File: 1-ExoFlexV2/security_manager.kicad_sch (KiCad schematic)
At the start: 5 parts, among them U15 OR GATE 3IN, U8 OR Gate 8, U9 OR Gate 8

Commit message: PLacement 2
- Puissance
- signaux
-
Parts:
- added J82: Jumper, Connector_PinHeader_2.54mm:PinHeader_1x03_P2.54mm_Vertical, symbol Connector:Conn_01x03_Male
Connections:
- net ALIM_SEC: now also J82.2 (Pin_2); no longer TP24.TP, U15.4 (Y)
- net GND: now also J82.3 (Pin_3)
- new net: J82.1 (Pin_1), TP24.TP, U15.4 (Y)
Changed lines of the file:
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@@
 (kicad_sch (version 20211123) (generator eeschema)
   (paper "A4")
+  (junction (at 228.6 93.98) (diameter 0) (color 0 0 0 0)
+  )
   (junction (at 130.81 121.92) (diameter 0) (color 0 0 0 0)
-  )
-  (junction (at 228.6 93.98) (diameter 0) (color 0 0 0 0)
   )
   (junction (at 130.81 124.46) (diameter 0) (color 0 0 0 0)
@@
     (stroke (width 0) (type default) (color 0 0 0 0))
   )
+  (wire (pts (xy 243.84 93.98) (xy 243.84 97.79))
+    (stroke (width 0) (type default) (color 0 0 0 0))
+  )
   (wire (pts (xy 77.47 120.65) (xy 87.63 120.65))
     (stroke (width 0) (type default) (color 0 0 0 0))
@@
   )
   (wire (pts (xy 182.88 73.66) (xy 182.88 91.44))
+    (stroke (width 0) (type default) (color 0 0 0 0))
+  )
+  (wire (pts (xy 246.38 97.79) (xy 251.46 97.79))
     (stroke (width 0) (type default) (color 0 0 0 0))
   )
@@
     (stroke (width 0.5) (type dash) (color 54 168 53 1))
   )
+  (wire (pts (xy 241.3 93.98) (xy 228.6 93.98))
+    (stroke (width 0) (type default) (color 0 0 0 0))
+  )
   (wire (pts (xy 77.47 67.31) (xy 82.55 67.31))
     (stroke (width 0) (type default) (color 0 0 0 0))
@@
     (stroke (width 0) (type default) (color 0 0 0 0))
   )
+  (wire (pts (xy 241.3 97.79) (xy 241.3 93.98))
+    (stroke (width 0) (type default) (color 0 0 0 0))
+  )
   (wire (pts (xy 130.81 119.38) (xy 132.08 119.38))
     (stroke (width 0) (type default) (color 0 0 0 0))
@@
   )
   (wire (pts (xy 149.86 106.68) (xy 152.4 106.68))
-    (stroke (width 0) (type default) (color 0 0 0 0))
-  )
-  (wire (pts (xy 228.6 93.98) (xy 238.76 93.98))
     (stroke (width 0) (type default) (color 0 0 0 0))
   )
@@
     )
   )
-  (global_label "ALIM_SEC" (shape input) (at 238.76 93.98 0) (fields_autoplaced)
+  (global_label "ALIM_SEC" (shape input) (at 243.84 93.98 0) (fields_autoplaced)
     (effects (font (size 1.27 1.27) (thickness 0.254) bold) (justify left))
-    (property "Intersheet References" "${INTERSHEET_REFS}" (id 0) (at 250.323 93.853 0)
+    (property "Intersheet References" "${INTERSHEET_REFS}" (id 0) (at 255.403 93.853 0)
       (effects (font (size 1.27 1.27) (thickness 0.254) bold) (justify left) hide)
     )
@@
       (effects (font (size 1.27 1.27)) hide)
     )
+    (pin "1")
+  )
+  (symbol (lib_id "Connector:Conn_01x03_Male") (at 243.84 102.87 90) (unit 1)
+    (in_bom yes) (on_board yes)
+    (property "Reference" "J82" (id 0) (at 238.76 101.6 90))
+    (property "Value" "Jumper" (id 1) (at 243.84 104.14 90))
+    (property "Footprint" "Connector_PinHeader_2.54mm:PinHeader_1x03_P2.54mm_Vertical" (id 2) (at 243.84 102.87 0)
+      (effects (font (size 1.27 1.27)) hide)
+    )
+    (property "Datasheet" "~" (id 3) (at 243.84 102.87 0)
+      (effects (font (size 1.27 1.27)) hide)
+    )
+    (property "DESCRIPTION" "CONN HEADER VERT 3POS 2.54MM" (id 4) (at 243.84 102.87 0)
+      (effects (font (size 1.27 1.27)) hide)
+    )
+    (property "MANUFACTURER" "Würth Elektronik" (id 5) (at 243.84 102.87 0)
+      (effects (font (size 1.27 1.27)) hide)
+    )
+    (property "PACKAGE" "Square 0.100\" (2.54mm)" (id 6) (at 243.84 102.87 0)
+      (effects (font (size 1.27 1.27)) hide)
+    )
+    (property "PART NUMBER" "61300311121" (id 7) (at 243.84 102.87 0)
+      (effects (font (size 1.27 1.27)) hide)
+    )
+    (property "TYPE" "Through Hole" (id 8) (at 243.84 102.87 0)
+      (effects (font (size 1.27 1.27)) hide)
+    )
+    (pin "1")
+    (pin "2")
+    (pin "3")
+  )
+  (symbol (lib_id "power:GND") (at 251.46 97.79 0) (unit 1)
+    (in_bom yes) (on_board yes)
+    (property "Reference" "#PWR0521" (id 0) (at 251.46 104.14 0)
+      (effects (font (size 1.27 1.27)) hide)
+    )
+    (property "Value" "GND" (id 1) (at 251.46 101.6 0))
+    (property "Footprint" "" (id 2) (at 251.46 97.79 0)
+      (effects (font (size 1.27 1.27)) hide)
+    )
+    (property "Datasheet" "" (id 3) (at 251.46 97.79 0)
+      (effects (font (size 1.27 1.27)) hide)
+    )

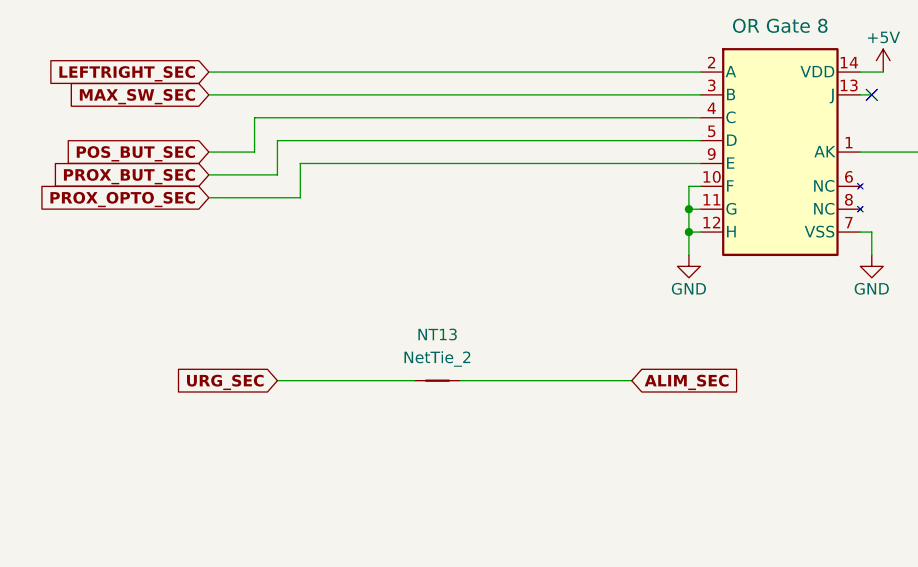
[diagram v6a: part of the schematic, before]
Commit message: Routage Fin
- Alimentation router
- Urg Sec dans le OR gate vers Alim Sec
- Changement d'un condo
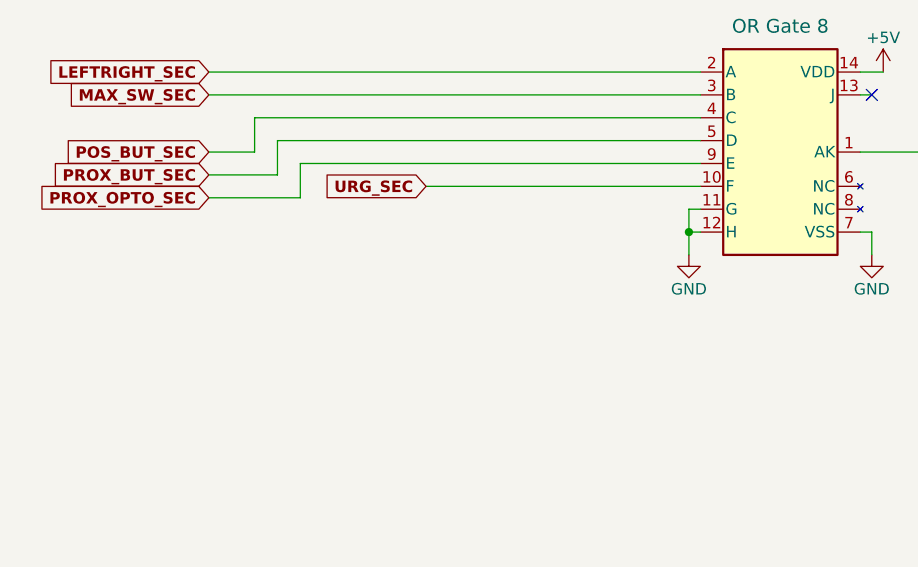
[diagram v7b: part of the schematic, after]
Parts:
- removed NT13: NetTie_2, NetTie:NetTie-2_THT_Pad0.3mm, symbol Device:NetTie_2
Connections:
- net GND: no longer U9.10 (F)
- net URG_SEC: now also U9.10 (F)
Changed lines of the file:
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@@
   (junction (at 228.6 93.98) (diameter 0) (color 0 0 0 0)
-  )
-  (junction (at 130.81 121.92) (diameter 0) (color 0 0 0 0)
   )
   (junction (at 130.81 124.46) (diameter 0) (color 0 0 0 0)
@@
     (stroke (width 0) (type default) (color 0 0 0 0))
   )
-  (wire (pts (xy 130.81 121.92) (xy 130.81 119.38))
-    (stroke (width 0) (type default) (color 0 0 0 0))
-  )
   (wire (pts (xy 80.01 69.85) (xy 80.01 72.39))
     (stroke (width 0) (type default) (color 0 0 0 0))
@@
     (stroke (width 0) (type default) (color 0 0 0 0))
   )
-  (wire (pts (xy 105.41 140.97) (xy 124.46 140.97))
-    (stroke (width 0) (type default) (color 0 0 0 0))
-  )
   (wire (pts (xy 151.13 109.22) (xy 149.86 109.22))
     (stroke (width 0) (type default) (color 0 0 0 0))
@@
   )
   (wire (pts (xy 241.3 97.79) (xy 241.3 93.98))
-    (stroke (width 0) (type default) (color 0 0 0 0))
-  )
-  (wire (pts (xy 130.81 119.38) (xy 132.08 119.38))
     (stroke (width 0) (type default) (color 0 0 0 0))
   )
@@
     (stroke (width 0.5) (type dash) (color 54 168 53 1))
   )
-  (wire (pts (xy 85.09 140.97) (xy 100.33 140.97))
+  (wire (pts (xy 101.6 119.38) (xy 132.08 119.38))
     (stroke (width 0) (type default) (color 0 0 0 0))
   )
@@
     )
   )
-  (global_label "URG_SEC" (shape input) (at 85.09 140.97 180) (fields_autoplaced)
-    (effects (font (size 1.27 1.27) (thickness 0.254) bold) (justify right))
-    (property "Intersheet References" "${INTERSHEET_REFS}" (id 0) (at 73.8293 141.097 0)
+  (global_label "URG_SEC" (shape input) (at 101.6 119.38 180) (fields_autoplaced)
+    (effects (font (size 1.27 1.27) (thickness 0.254) bold) (justify right))
+    (property "Intersheet References" "${INTERSHEET_REFS}" (id 0) (at 90.3393 119.507 0)
       (effects (font (size 1.27 1.27) (thickness 0.254) bold) (justify right) hide)
     )
@@
     (effects (font (size 1.27 1.27) (thickness 0.254) bold) (justify left))
     (property "Intersheet References" "${INTERSHEET_REFS}" (id 0) (at 255.403 93.853 0)
-      (effects (font (size 1.27 1.27) (thickness 0.254) bold) (justify left) hide)
-    )
-  )
-  (global_label "ALIM_SEC" (shape input) (at 124.46 140.97 0) (fields_autoplaced)
-    (effects (font (size 1.27 1.27) (thickness 0.254) bold) (justify left))
-    (property "Intersheet References" "${INTERSHEET_REFS}" (id 0) (at 136.023 140.843 0)
       (effects (font (size 1.27 1.27) (thickness 0.254) bold) (justify left) hide)
     )
@@
     (pin "1")
   )
-  (symbol (lib_id "Device:NetTie_2") (at 102.87 140.97 0) (unit 1)
-    (in_bom no) (on_board yes) (fields_autoplaced)
-    (property "Reference" "NT13" (id 0) (at 102.87 135.89 0))
-    (property "Value" "NetTie_2" (id 1) (at 102.87 138.43 0))
-    (property "Footprint" "NetTie:NetTie-2_THT_Pad0.3mm" (id 2) (at 102.87 140.97 0)
-      (effects (font (size 1.27 1.27)) hide)
-    )
-    (property "Datasheet" "~" (id 3) (at 102.87 140.97 0)
-      (effects (font (size 1.27 1.27)) hide)
-    )
-    (pin "1")
-    (pin "2")
-  )
   (symbol (lib_id "power:GND") (at 130.81 127 0) (unit 1)

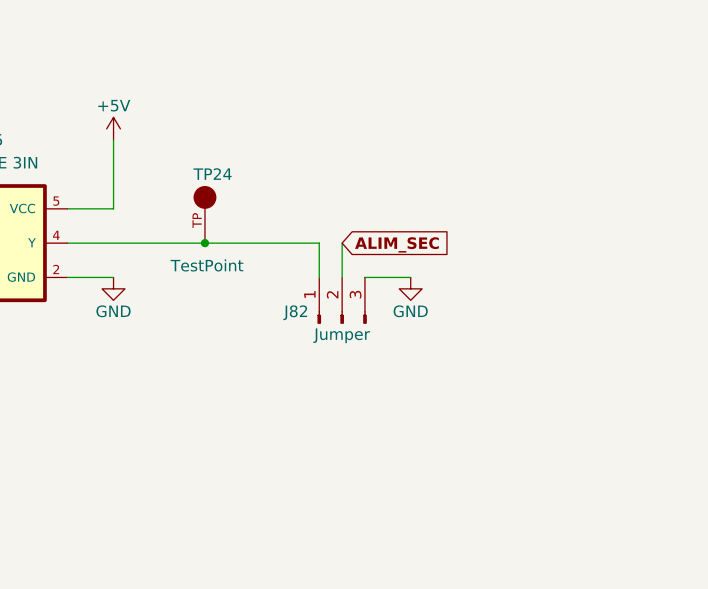
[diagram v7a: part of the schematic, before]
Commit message: Routage pour Review 1
- Replacement des test point pour faciliter le rework
- Correction des erreurs dans le BOM
-
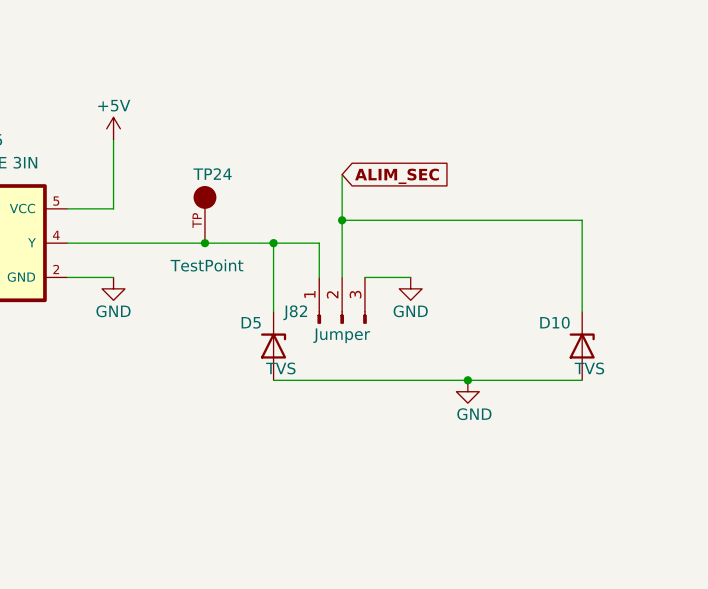
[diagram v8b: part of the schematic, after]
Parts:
- added D10, D5: TVS, FootPrint:DPY2_TEX, symbol Device:D_Zener
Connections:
- net ALIM_SEC: now also D10.1 (K)
- net GND: now also D10.2 (A), D5.2 (A)
- net at J82.1 (Pin_1), TP24.TP, U15.4 (Y): now also D5.1 (K)
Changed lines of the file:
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@@
 (kicad_sch (version 20211123) (generator eeschema)
   (paper "A4")
+  (junction (at 243.84 91.44) (diameter 0) (color 0 0 0 0)
+  )
   (junction (at 228.6 93.98) (diameter 0) (color 0 0 0 0)
+  )
+  (junction (at 236.22 93.98) (diameter 0) (color 0 0 0 0)
+  )
+  (junction (at 257.81 109.22) (diameter 0) (color 0 0 0 0)
   )
   (junction (at 130.81 124.46) (diameter 0) (color 0 0 0 0)
@@
   (no_connect (at 151.13 109.22))
   (no_connect (at 149.86 67.31))
+  (wire (pts (xy 270.51 101.6) (xy 270.51 91.44))
+    (stroke (width 0) (type default) (color 0 0 0 0))
+  )
   (wire (pts (xy 130.81 124.46) (xy 132.08 124.46))
     (stroke (width 0) (type default) (color 0 0 0 0))
   )
-  (wire (pts (xy 243.84 93.98) (xy 243.84 97.79))
+  (wire (pts (xy 243.84 86.36) (xy 243.84 91.44))
     (stroke (width 0) (type default) (color 0 0 0 0))
   )
@@
     (stroke (width 0) (type default) (color 0 0 0 0))
   )
+  (wire (pts (xy 236.22 109.22) (xy 257.81 109.22))
+    (stroke (width 0) (type default) (color 0 0 0 0))
+  )
+  (wire (pts (xy 243.84 91.44) (xy 270.51 91.44))
+    (stroke (width 0) (type default) (color 0 0 0 0))
+  )
   (wire (pts (xy 87.63 120.65) (xy 87.63 116.84))
     (stroke (width 0) (type default) (color 0 0 0 0))
@@
   )
   (wire (pts (xy 182.88 73.66) (xy 182.88 91.44))
+    (stroke (width 0) (type default) (color 0 0 0 0))
+  )
+  (wire (pts (xy 243.84 91.44) (xy 243.84 97.79))
     (stroke (width 0) (type default) (color 0 0 0 0))
   )
@@
     (stroke (width 0.5) (type dash) (color 54 168 53 1))
   )
-  (wire (pts (xy 241.3 93.98) (xy 228.6 93.98))
-    (stroke (width 0) (type default) (color 0 0 0 0))
-  )
   (wire (pts (xy 77.47 67.31) (xy 82.55 67.31))
     (stroke (width 0) (type default) (color 0 0 0 0))
@@
     (stroke (width 0) (type default) (color 0 0 0 0))
   )
+  (wire (pts (xy 257.81 109.22) (xy 270.51 109.22))
+    (stroke (width 0) (type default) (color 0 0 0 0))
+  )
   (wire (pts (xy 213.36 93.98) (xy 228.6 93.98))
     (stroke (width 0) (type default) (color 0 0 0 0))
@@
   )
   (wire (pts (xy 77.47 80.01) (xy 82.55 80.01))
+    (stroke (width 0) (type default) (color 0 0 0 0))
+  )
+  (wire (pts (xy 236.22 93.98) (xy 228.6 93.98))
     (stroke (width 0) (type default) (color 0 0 0 0))
   )
@@
     (stroke (width 0) (type default) (color 0 0 0 0))
   )
-  (wire (pts (xy 241.3 97.79) (xy 241.3 93.98))
+  (wire (pts (xy 241.3 93.98) (xy 241.3 97.79))
     (stroke (width 0) (type default) (color 0 0 0 0))
   )
@@
     (stroke (width 0.5) (type dash) (color 54 168 53 1))
   )
+  (wire (pts (xy 236.22 101.6) (xy 236.22 93.98))
+    (stroke (width 0) (type default) (color 0 0 0 0))
+  )
   (wire (pts (xy 87.63 116.84) (xy 132.08 116.84))
     (stroke (width 0) (type default) (color 0 0 0 0))
@@
   )
   (wire (pts (xy 77.47 88.9) (xy 87.63 88.9))
+    (stroke (width 0) (type default) (color 0 0 0 0))
+  )
+  (wire (pts (xy 236.22 93.98) (xy 241.3 93.98))
     (stroke (width 0) (type default) (color 0 0 0 0))
   )
@@
     )
   )
-  (global_label "ALIM_SEC" (shape input) (at 243.84 93.98 0) (fields_autoplaced)
+  (global_label "ALIM_SEC" (shape input) (at 243.84 86.36 0) (fields_autoplaced)
     (effects (font (size 1.27 1.27) (thickness 0.254) bold) (justify left))
-    (property "Intersheet References" "${INTERSHEET_REFS}" (id 0) (at 255.403 93.853 0)
+    (property "Intersheet References" "${INTERSHEET_REFS}" (id 0) (at 255.403 86.233 0)
       (effects (font (size 1.27 1.27) (thickness 0.254) bold) (justify left) hide)
     )
@@
     (pin "9")
   )
+  (symbol (lib_id "power:GND") (at 257.81 109.22 0) (unit 1)
+    (in_bom yes) (on_board yes)
+    (property "Reference" "#PWR0339" (id 0) (at 257.81 115.57 0)
+      (effects (font (size 1.27 1.27)) hide)
+    )
+    (property "Value" "GND" (id 1) (at 256.54 113.03 0)
+      (effects (font (size 1.27 1.27)) (justify left))
+    )
+    (property "Footprint" "" (id 2) (at 257.81 109.22 0)
+      (effects (font (size 1.27 1.27)) hide)
+    )
+    (property "Datasheet" "" (id 3) (at 257.81 109.22 0)
+      (effects (font (size 1.27 1.27)) hide)
+    )
+    (pin "1")
+  )
   (symbol (lib_id "SymLib:SN74LVC1G332DBVR") (at 204.47 99.06 0) (unit 1)
     (in_bom yes) (on_board yes) (fields_autoplaced)
@@
     (pin "1")
   )
+  (symbol (lib_id "Device:D_Zener") (at 270.51 105.41 270) (unit 1)
+    (in_bom yes) (on_board yes)
+    (property "Reference" "D10" (id 0) (at 269.24 102.87 90)
+      (effects (font (size 1.27 1.27)) (justify right))
+    )
+    (property "Value" "TVS" (id 1) (at 273.05 107.95 90)
+      (effects (font (size 1.27 1.27)) (justify right))
+    )
+    (property "Footprint" "FootPrint:DPY2_TEX" (id 2) (at 270.51 105.41 0)
+      (effects (font (size 1.27 1.27)) hide)
+    )
+    (property "Datasheet" "~" (id 3) (at 270.51 105.41 0)
+      (effects (font (size 1.27 1.27)) hide)
+    )
+    (property "DESCRIPTION" "TVS DIODE 5.5VWM 14VC 2X1SON" (id 4) (at 270.51 105.41 0)
+      (effects (font (size 1.27 1.27)) hide)
+    )
+    (property "MANUFACTURER" "Texas Instruments" (id 5) (at 270.51 105.41 0)
+      (effects (font (size 1.27 1.27)) hide)
+    )
+    (property "PACKAGE" "0402 (1006 Metric)" (id 6) (at 270.51 105.41 0)
+      (effects (font (size 1.27 1.27)) hide)
+    )
+    (property "PART NUMBER" "TPD1E05U06DPYR" (id 7) (at 270.51 105.41 0)
+      (effects (font (size 1.27 1.27)) hide)
+    )
+    (property "TYPE" "SMD" (id 8) (at 270.51 105.41 0)
+      (effects (font (size 1.27 1.27)) hide)
+    )
+    (pin "1")
+    (pin "2")
+  )
+  (symbol (lib_id "Device:D_Zener") (at 236.22 105.41 270) (unit 1)
+    (in_bom yes) (on_board yes)
+    (property "Reference" "D5" (id 0) (at 234.95 102.87 90)
+      (effects (font (size 1.27 1.27)) (justify right))
+    )
+    (property "Value" "TVS" (id 1) (at 238.76 107.95 90)
+      (effects (font (size 1.27 1.27)) (justify right))
+    )
+    (property "Footprint" "FootPrint:DPY2_TEX" (id 2) (at 236.22 105.41 0)
+      (effects (font (size 1.27 1.27)) hide)
+    )
+    (property "Datasheet" "~" (id 3) (at 236.22 105.41 0)
+      (effects (font (size 1.27 1.27)) hide)
+    )
+    (property "DESCRIPTION" "TVS DIODE 5.5VWM 14VC 2X1SON" (id 4) (at 236.22 105.41 0)
+      (effects (font (size 1.27 1.27)) hide)
+    )
+    (property "MANUFACTURER" "Texas Instruments" (id 5) (at 236.22 105.41 0)
+      (effects (font (size 1.27 1.27)) hide)
+    )
+    (property "PACKAGE" "0402 (1006 Metric)" (id 6) (at 236.22 105.41 0)
+      (effects (font (size 1.27 1.27)) hide)
+    )
+    (property "PART NUMBER" "TPD1E05U06DPYR" (id 7) (at 236.22 105.41 0)
+      (effects (font (size 1.27 1.27)) hide)
+    )
+    (property "TYPE" "SMD" (id 8) (at 236.22 105.41 0)
+      (effects (font (size 1.27 1.27)) hide)
+    )
+    (pin "1")
+    (pin "2")
+  )
   (symbol (lib_id "SymLib:CD4078BM96") (at 113.03 64.77 0) (unit 1)
